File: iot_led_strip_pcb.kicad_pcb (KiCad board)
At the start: 2 copper layers, 50 x 50 mm, 58 parts, among them J1 I2C Expansion, J2 Conn_01x03_Socket, J3 GT-USB-7010ASV, J4 Barrel_Jack_Switch_Pin3Ring, J5 TC2050-IDC_Cortex-M, J6 Conn_01x03_Socket_Solderwire, J8 UART, Q1 BSS138, SW1 RESET, SW2 FLASH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

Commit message: lots of small changes. Schematic updated with mic, layout not yet
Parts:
- removed C8, C9: 47pF, Capacitor_SMD:C_0805_2012Metric_Pad1.18x1.45mm_HandSolder
- added J7: PWR_HEADER, Connector_Wire:SolderWire-0.1sqmm_1x02_P3.6mm_D0.4mm_OD1mm, F.Cu at (119.9, 89.1)
- moved C14 2.25 mm to (125.4, 109.0)
- moved R4 2.25 mm to (130.0, 109.0)
- moved R5 2.25 mm to (127.8, 109.0)
- moved R3 2.10 mm to (123.1, 104.2)
- moved R10 2.10 mm to (123.1, 109.0)
- moved TP5 2.09 mm to (125.4, 104.4)
- moved TP4 2.05 mm to (128.6, 104.6)
- moved SW2 0.27 mm to (137.2, 115.2)
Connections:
- J1 pad 3: /SDA -> /SCL
- J1 pad 4: /SCL -> /SDA
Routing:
- net Earth: track 139.4 -> 119.4 mm
- net +5V: track 71.3 -> 77.8 mm
- net /SDA: track 49.8 -> 45.4 mm
- net /SCL: track 48.2 -> 51.3 mm
- net /USB_D-: track 23.2 -> 26.1 mm
- net /USB_D+: track 22.5 -> 25.0 mm
- net BOOT: track 15.1 -> 17.4 mm
- net +3.3V: track 138.3 -> 139.7 mm
- net /DP: track 10.7 -> 9.30 mm
- net /DN: track 11.6 -> 10.5 mm
- added copper zone on B.Cu, net +5V
- added copper zone on F.Cu, net +5V
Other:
- board text added: "0xjmux"
- board text added: "v2.1 10-2023"
- board text removed: "0xjmux & tsnl"
- board text removed: "v2.0 09-2023"

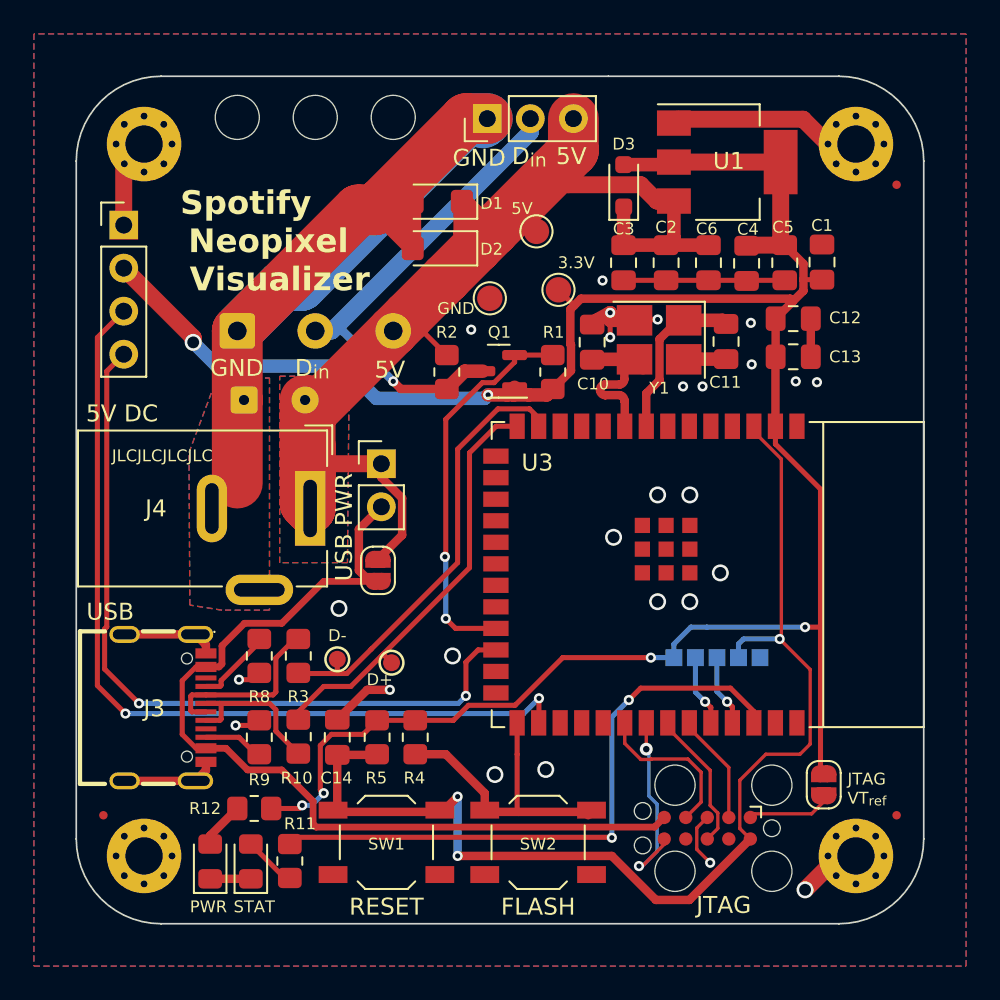
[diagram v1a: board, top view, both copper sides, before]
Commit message: microphone added to layout, DRC passes
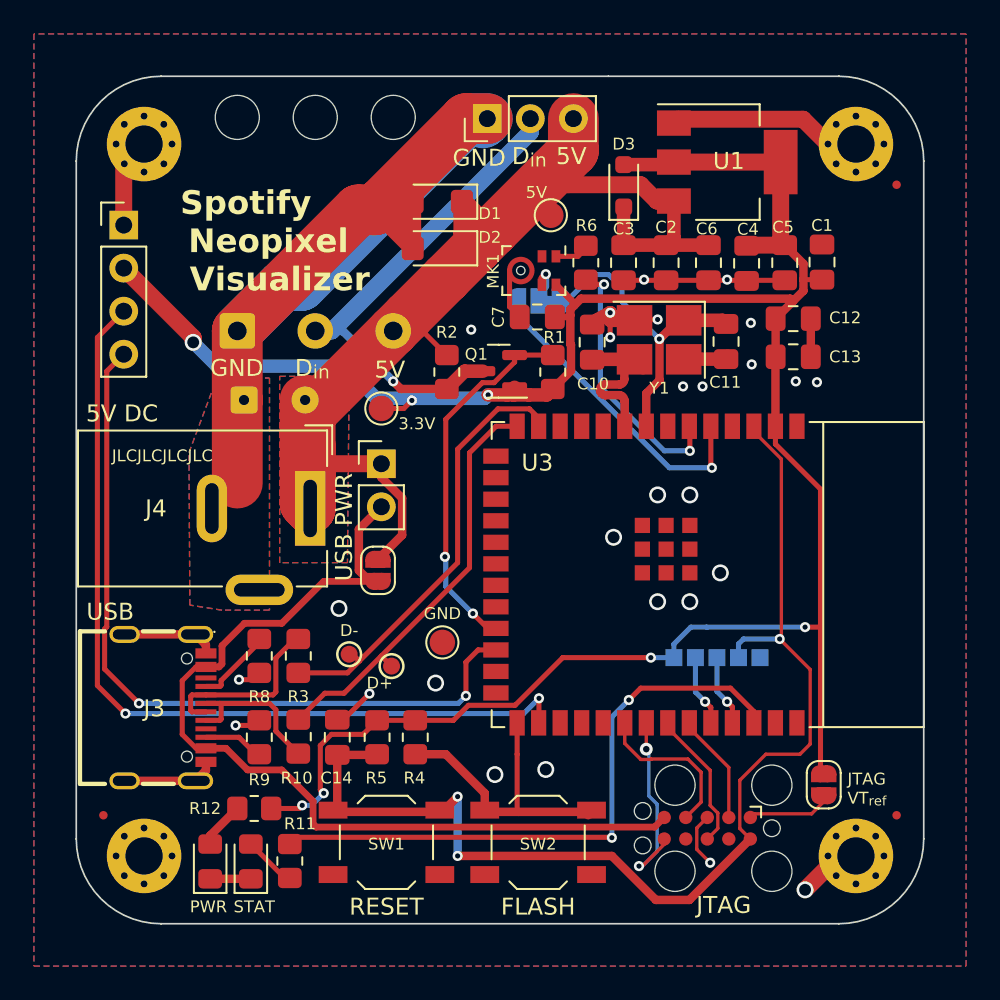
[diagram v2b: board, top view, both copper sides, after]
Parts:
- added C7: 100nF, Capacitor_SMD:C_0805_2012Metric_Pad1.18x1.45mm_HandSolder, F.Cu at (137.2, 84.2)
- added JP1: MIC_CLK_SEL, Jumper:SolderJumper-3_P1.3mm_Bridged12_RoundedPad1.0x1.5mm, B.Cu at (137.3, 83.3)
- added MK1: SPH0641LU4H-1, Sensor_Audio:Knowles_LGA-5_3.5x2.65mm, F.Cu at (137.0, 81.5)
- added R6: 100, Resistor_SMD:R_0805_2012Metric_Pad1.20x1.40mm_HandSolder, F.Cu at (140.1, 81.0)
- moved TP3 20.5 mm to (131.6, 103.4)
- moved TP2 12.6 mm to (128.0, 89.6)
- moved TP1 1.27 mm to (138.0, 78.2)
- moved TP5 0.76 mm to (126.1, 104.1)
- moved TP4 0.20 mm to (128.6, 104.8)
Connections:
- U3 pad 5: unconnected-(U3-GPIO5/TOUCH5/ADC1_CH4-Pad5) -> /MIC_CLK
- U3 pad 6: unconnected-(U3-GPIO6/TOUCH6/ADC1_CH5-Pad6) -> /MIC_DATA
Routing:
- net /MIC_CLK: track 0.00 -> 18.2 mm, vias 0 -> 1
- net /MIC_DATA: track 0.00 -> 15.6 mm, vias 0 -> 2
- net /XP: track 9.94 -> 18.6 mm, vias 0 -> 1
- net +3.3V: track 139.7 -> 143.0 mm, vias 6 -> 7
- net Net-(JP1-C): track 0.00 -> 2.81 mm, vias 0 -> 1
- net Net-(MK1-DATA): track 0.00 -> 1.96 mm
- net Earth: track 119.4 -> 121.1 mm, vias 26 -> 27
- net /LV_DIN: track 23.1 -> 22.0 mm
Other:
- board text added: "ESP"
- board text added: "MIC CLK SEL"
- board text added: "MIC!"
- board text added: "Y1"
- board text removed: "0xjmux"
- board text removed: "v2.1 10-2023"

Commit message: v2.1 export, renders
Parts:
- moved D3 0.52 mm to (142.4, 76.0)
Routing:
- net +5V: track 77.8 -> 75.6 mm
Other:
- board text added: "0xjmux"
- board text added: "LED STRIP PWR"
- board text added: "v2.1 10-2023"

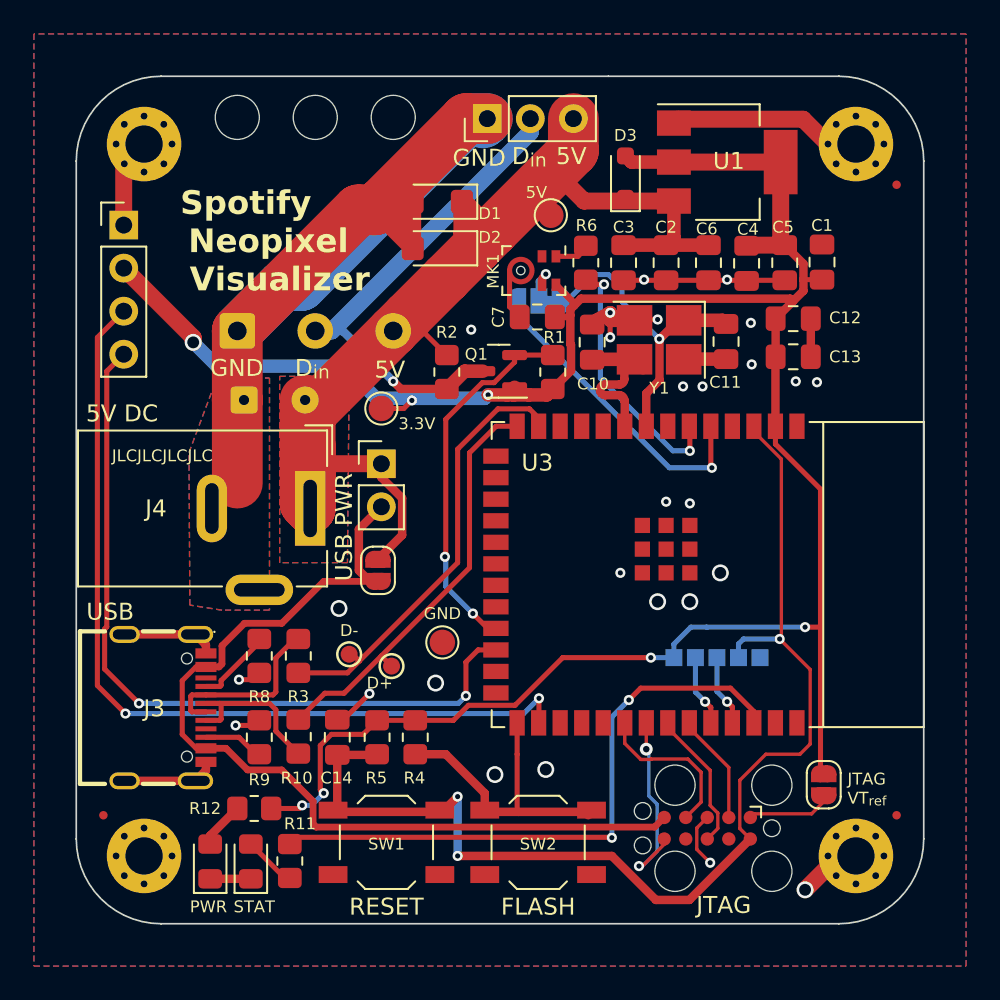
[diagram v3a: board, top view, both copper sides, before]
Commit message: replaced crystal. re-updated all renders and images
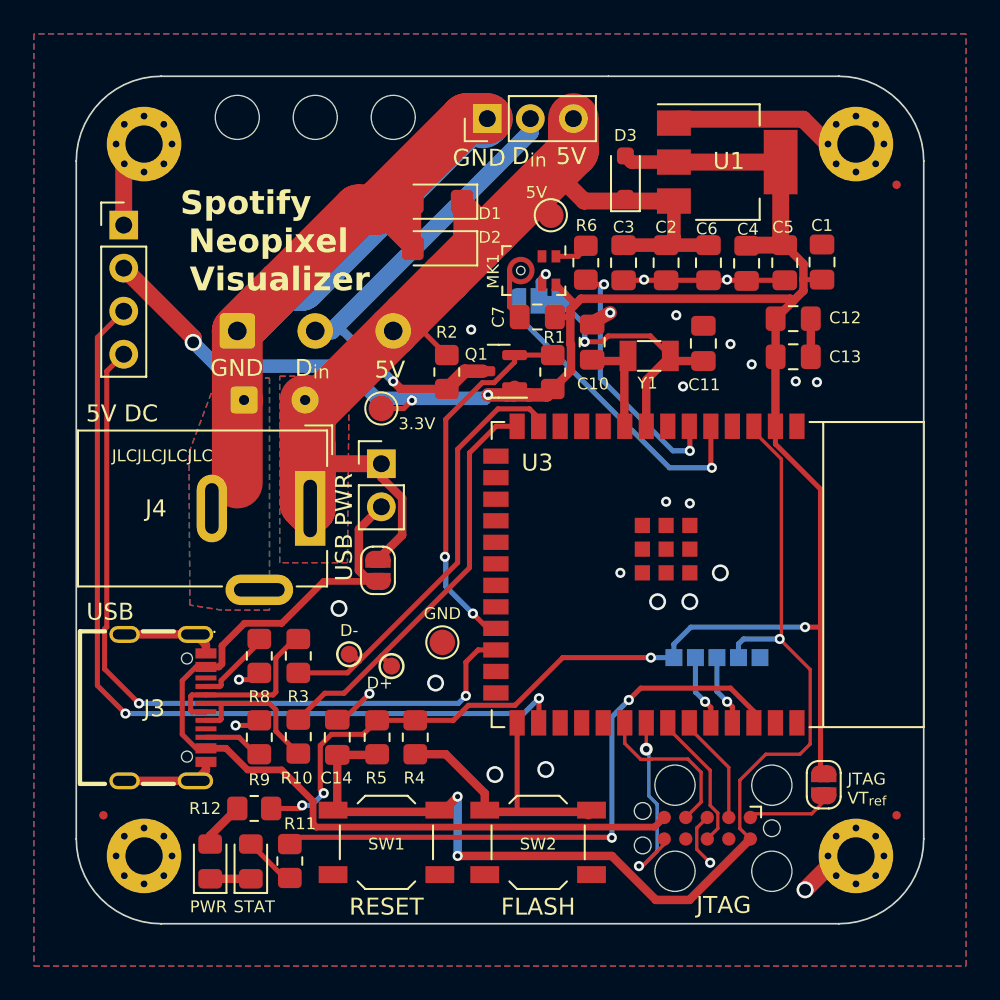
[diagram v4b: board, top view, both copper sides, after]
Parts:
- Y1: value Crystal_32Khz -> Crystal 32kHz; footprint Crystal:Crystal_SMD_3225-4Pin_3.2x2.5mm_HandSoldering -> Crystal:Crystal_SMD_3215-2Pin_3.2x1.5mm
- moved C11 1.34 mm to (147.0, 85.8), turned to 90 degrees
- moved Y1 1.12 mm to (143.8, 86.5), turned to 0 degrees
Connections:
- Y1 pad 2: Earth -> /XN
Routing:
- net Earth: track 121.1 -> 110.1 mm, vias 27 -> 25
- net /XN: track 9.68 -> 5.49 mm
- net /XP: track 18.6 -> 15.5 mm
- net /~{RST}: track 69.1 -> 68.3 mm
- net /USB_D-: track 26.1 -> 25.3 mm
- net Net-(U3-GPIO2/TOUCH2/ADC1_CH1): track 36.6 -> 36.1 mm

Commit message: re-re-updated photos & board
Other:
- board text added: "0xjmux & tsnl"
- board text removed: "0xjmux"
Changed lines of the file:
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@@
     (effects (font (size 0.7 0.7) (thickness 0.11)) (justify left bottom mirror))
   )
-  (gr_text "0xjmux" (at 145.4 95.9) (layer "B.SilkS")
+  (gr_text "0xjmux & tsnl" (at 148.3 95.9) (layer "B.SilkS")
     (effects (font (size 1 1) (thickness 0.15)) (justify left bottom mirror))
   )
@@
   (segment (start 126.644785 77.880215) (end 127.619785 77.880215) (width 3) (layer "F.Cu") (net 1))
   (via (at 134.7 111.2) (size 1) (drill 0.7) (layers "F.Cu" "B.Cu") (free) (net 1))
-  (via (at 146.2 95.2) (size 0.6) (drill 0.3) (layers "F.Cu" "B.Cu") (free) (net 1))
+  (via (at 145.8 94.9) (size 0.6) (drill 0.3) (layers "F.Cu" "B.Cu") (free) (net 1))
   (via (at 145.8 88.3) (size 0.6) (drill 0.3) (layers "F.Cu" "B.Cu") (free) (net 1))
   (via (at 145.4 84.1) (size 0.6) (drill 0.3) (layers "F.Cu" "B.Cu") (free) (net 1))
   (via (at 148 99.3) (size 1) (drill 0.7) (layers "F.Cu" "B.Cu") (free) (net 1))
   (via (at 127.3 106.4235) (size 0.6) (drill 0.3) (layers "F.Cu" "B.Cu") (net 1))
-  (via (at 144.8 95.1) (size 0.6) (drill 0.3) (layers "F.Cu" "B.Cu") (free) (net 1))
+  (via (at 144.7 94.9) (size 0.6) (drill 0.3) (layers "F.Cu" "B.Cu") (free) (net 1))
   (via (at 141.5 83.95) (size 0.6) (drill 0.3) (layers "F.Cu" "B.Cu") (net 1))
   (via (at 119.4 108.3) (size 0.6) (drill 0.3) (layers "F.Cu" "B.Cu") (free) (net 1))

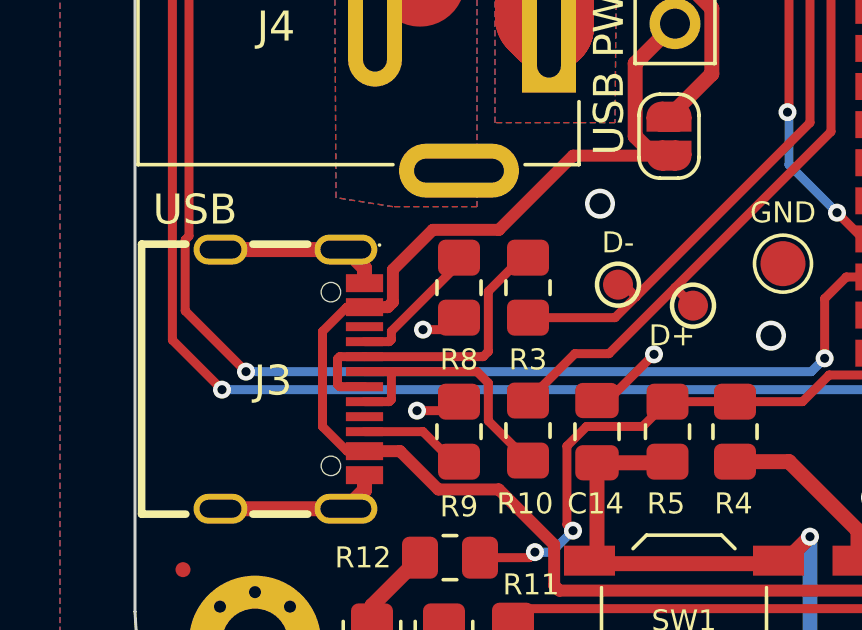
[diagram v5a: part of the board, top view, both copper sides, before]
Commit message: some minor changes from during assembly and gif of assembled board added
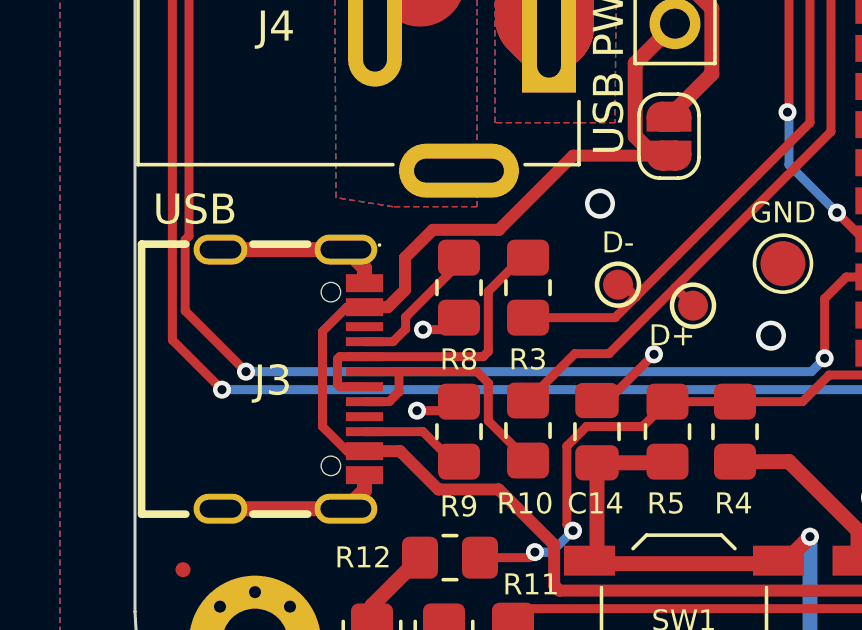
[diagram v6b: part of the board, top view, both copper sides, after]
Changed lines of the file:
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@@
   (segment (start 151.5 103.2) (end 149.37 103.2) (width 0.3) (layer "B.Cu") (net 6))
   (segment (start 120.110999 110.927) (end 118.834024 109.650025) (width 0.4) (layer "F.Cu") (net 7))
-  (segment (start 127.8 99.8) (end 124.602749 99.8) (width 0.4) (layer "F.Cu") (net 7))
-  (segment (start 119.927 102.273) (end 118.597027 103.602973) (width 0.4) (layer "F.Cu") (net 7))
   (segment (start 117.650025 109.650025) (end 117.071123 109.650025) (width 0.3) (layer "F.Cu") (net 7))
-  (segment (start 118.597027 104.677076) (end 118.424179 104.849924) (width 0.4) (layer "F.Cu") (net 7))
+  (segment (start 119 104.274103) (end 118.424179 104.849924) (width 0.4) (layer "F.Cu") (net 7))
+  (segment (start 119.927 102.273) (end 119 103.2) (width 0.4) (layer "F.Cu") (net 7))
   (segment (start 117.061217 104.849924) (end 117.650025 104.849924) (width 0.3) (layer "F.Cu") (net 7))
   (segment (start 144.1217 114.2983) (end 124.1443 114.2983) (width 0.4) (layer "F.Cu") (net 7))
+  (segment (start 127.8 99.8) (end 124.602749 99.8) (width 0.4) (layer "F.Cu") (net 7))
   (segment (start 116.25 108.828902) (end 116.25 105.661141) (width 0.3) (layer "F.Cu") (net 7))
   (segment (start 144.69 113.73) (end 144.1217 114.2983) (width 0.4) (layer "F.Cu") (net 7))
@@
   (segment (start 117.071123 109.650025) (end 116.25 108.828902) (width 0.3) (layer "F.Cu") (net 7))
   (segment (start 126.673 96.727) (end 126.673 99.15616) (width 0.5) (layer "F.Cu") (net 7))
-  (segment (start 118.597027 103.602973) (end 118.597027 104.677076) (width 0.4) (layer "F.Cu") (net 7))
-  (segment (start 122.129749 102.273) (end 119.927 102.273) (width 0.4) (layer "F.Cu") (net 7))
   (segment (start 126.673 99.15616) (end 127.31684 99.8) (width 0.5) (layer "F.Cu") (net 7))
+  (segment (start 119 103.2) (end 119 104.274103) (width 0.4) (layer "F.Cu") (net 7))
   (segment (start 116.25 105.661141) (end 117.061217 104.849924) (width 0.3) (layer "F.Cu") (net 7))
-  (segment (start 124.602749 99.8) (end 122.129749 102.273) (width 0.4) (layer "F.Cu") (net 7))
   (segment (start 118.424179 104.849924) (end 117.650025 104.849924) (width 0.4) (layer "F.Cu") (net 7))
   (segment (start 118.834024 109.650025) (end 117.650025 109.650025) (width 0.4) (layer "F.Cu") (net 7))
   (segment (start 128 95.4) (end 126.673 96.727) (width 0.5) (layer "F.Cu") (net 7))
+  (segment (start 124.602749 99.8) (end 122.129749 102.273) (width 0.4) (layer "F.Cu") (net 7))
   (segment (start 122.127 110.927) (end 120.110999 110.927) (width 0.4) (layer "F.Cu") (net 7))
+  (segment (start 122.129749 102.273) (end 119.927 102.273) (width 0.4) (layer "F.Cu") (net 7))
   (segment (start 132.9125 87.4) (end 131.8625 88.45) (width 0.8) (layer "F.Cu") (net 8))
   (segment (start 128.7 88) (end 129.15 88.45) (width 0.5) (layer "F.Cu") (net 8))
@@
   (segment (start 134.877 89.623) (end 136.737 89.623) (width 0.3) (layer "F.Cu") (net 17))
   (segment (start 132.5 92) (end 134.877 89.623) (width 0.3) (layer "F.Cu") (net 17))
+  (segment (start 118.4739 108.000038) (end 117.650025 108.000038) (width 0.3) (layer "F.Cu") (net 18))
   (segment (start 121.777 108.6395) (end 123.1 109.9625) (width 0.3) (layer "F.Cu") (net 18))
   (segment (start 121.777 107.377) (end 121.777 108.6395) (width 0.3) (layer "F.Cu") (net 18))
-  (segment (start 118.474154 107.000038) (end 118.547027 107.072911) (width 0.3) (layer "F.Cu") (net 18))
+  (segment (start 118.8 107.673938) (end 118.4739 108.000038) (width 0.3) (layer "F.Cu") (net 18))
   (segment (start 121.4 107) (end 121.777 107.377) (width 0.3) (layer "F.Cu") (net 18))
-  (segment (start 118.4739 108.000038) (end 117.650025 108.000038) (width 0.3) (layer "F.Cu") (net 18))
   (segment (start 118.474192 107) (end 121.4 107) (width 0.3) (layer "F.Cu") (net 18))
-  (segment (start 118.547027 107.926911) (end 118.4739 108.000038) (width 0.3) (layer "F.Cu") (net 18))
+  (segment (start 118.8 107) (end 118.8 107.673938) (width 0.3) (layer "F.Cu") (net 18))
   (segment (start 117.650025 107.000038) (end 118.474154 107.000038) (width 0.3) (layer "F.Cu") (net 18))
   (segment (start 118.474154 107.000038) (end 118.474192 107) (width 0.3) (layer "F.Cu") (net 18))
-  (segment (start 118.547027 107.072911) (end 118.547027 107.926911) (width 0.3) (layer "F.Cu") (net 18))
   (segment (start 117.650025 106.499911) (end 116.82615 106.499911) (width 0.3) (layer "F.Cu") (net 19))
   (segment (start 116.75 107.424015) (end 116.825896 107.499911) (width 0.3) (layer "F.Cu") (net 19))
@@
   (segment (start 117.9 115.3) (end 117.9 114.8) (width 0.5) (layer "F.Cu") (net 22))
   (segment (start 117.9 114.8) (end 119.5 113.2) (width 0.5) (layer "F.Cu") (net 22))
-  (segment (start 117.650025 106.000038) (end 118.4739 106.000038) (width 0.3) (layer "F.Cu") (net 23))
-  (segment (start 118.547027 105.926911) (end 118.547027 105.652973) (width 0.3) (layer "F.Cu") (net 23))
-  (segment (start 118.547027 105.652973) (end 120.8 103.4) (width 0.3) (layer "F.Cu") (net 23))
-  (segment (start 118.4739 106.000038) (end 118.547027 105.926911) (width 0.3) (layer "F.Cu") (net 23))
+  (segment (start 119.023 105.577) (end 119.023 105.177) (width 0.3) (layer "F.Cu") (net 23))
+  (segment (start 118.599962 106.000038) (end 119.023 105.577) (width 0.3) (layer "F.Cu") (net 23))
+  (segment (start 119.023 105.177) (end 120.8 103.4) (width 0.3) (layer "F.Cu") (net 23))
+  (segment (start 117.650025 106.000038) (end 118.599962 106.000038) (width 0.3) (layer "F.Cu") (net 23))
   (segment (start 117.650025 109.000038) (end 119.600038 109.000038) (width 0.3) (layer "F.Cu") (net 25))
   (segment (start 119.600038 109.000038) (end 120.6 110) (width 0.3) (layer "F.Cu") (net 25))
